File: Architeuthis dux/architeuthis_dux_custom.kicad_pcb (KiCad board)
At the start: 2 copper layers, 129.9 x 95.6 mm, 20 parts

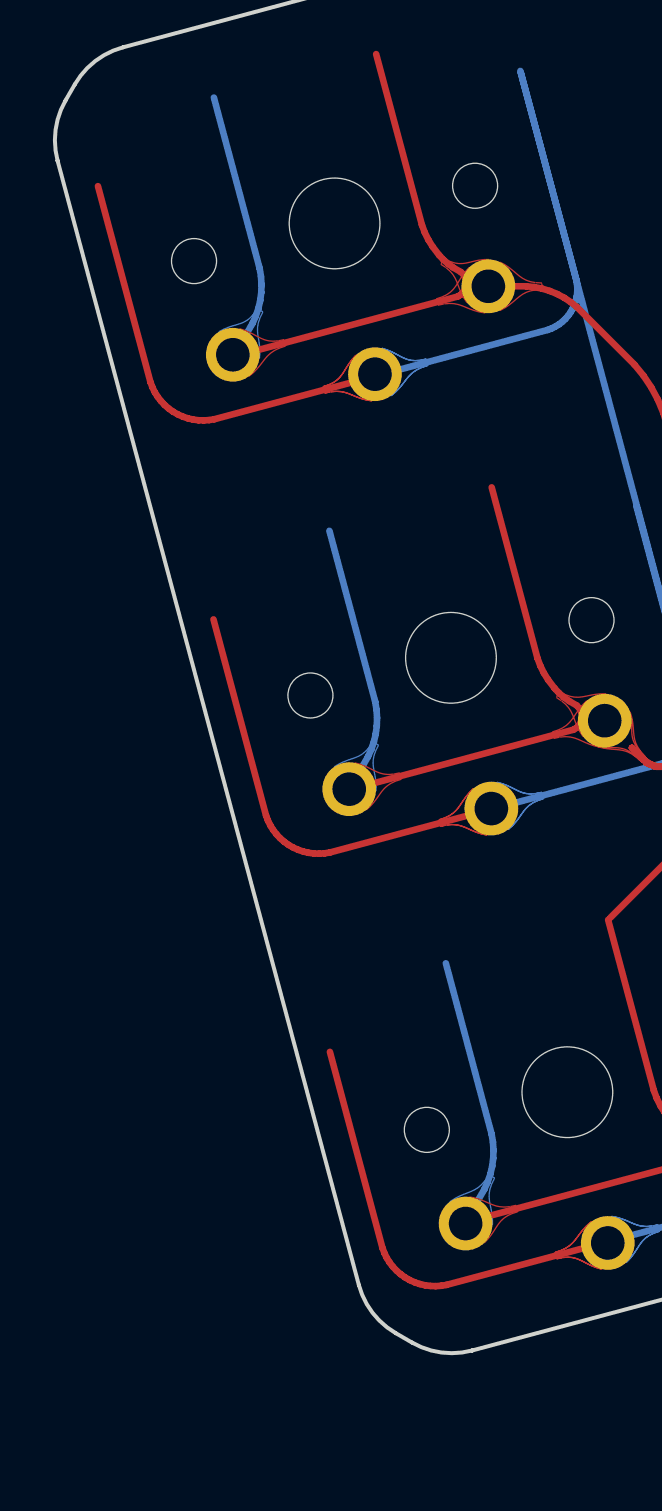
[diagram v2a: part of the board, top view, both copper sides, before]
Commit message: Remove phantom drill holes
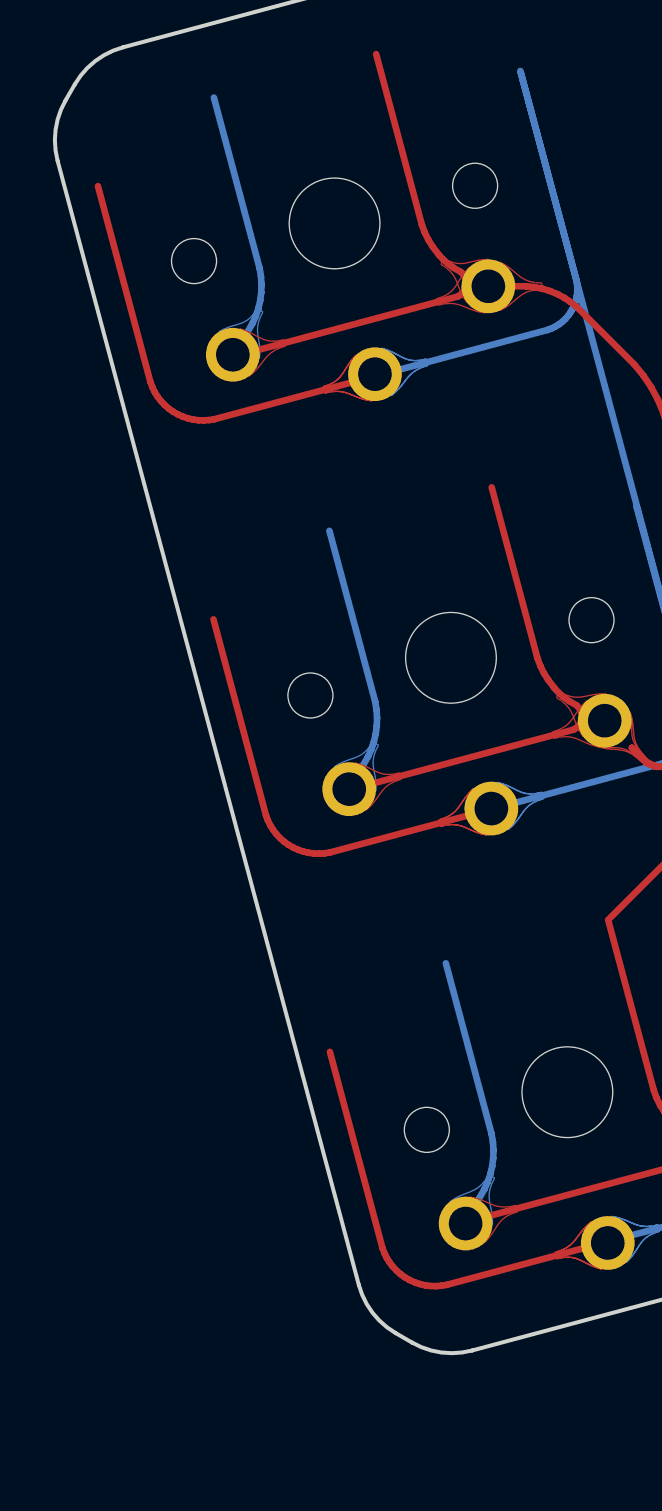
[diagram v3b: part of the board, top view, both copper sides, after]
